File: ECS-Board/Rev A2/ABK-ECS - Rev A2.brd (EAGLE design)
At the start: 80 x 80 mm, 169 parts, among them J1 22-27-2061-06, J2 USB-B-S-RA, J3 1241050-5, J4 MSTBA2, J5 22-05-7068-06, J6 22-05-7028-02, J7 22-05-7068-06, J8 22-05-7028-02, K1 G6K-2G-Y, SW1 B3FS-1015, SW2 B3FS-1015, T1 EXMACHINA-LOGO-NAME, T10 MMBT2222AL, T11 IRLML5103TRPBF, T2 IRLML5103TRPBF, T3 MMBT2222AL, T4 MMBT2222AL, T5 IRLML5103TRPBF, T6 MMBT2222AL, T7 IRLML5103TRPBF, T8 MMBT2222AL, T9 IRLML5103TRPBF, U1 AT24C512C-SSHM-B, U2 LPC1768FBD100, U3 LT3686HDDPBF, U4 LT3686HDDPBF, U5 CD4050BD, X1 FC-135, X2 ASE-12, X3 3000

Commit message: Add rev A2 and modify board
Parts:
- added R75: 1K5, rcl:R0603
- F1: value FUSE3557L -> 1812L110/24DR; device fuse2:3557-LITTLE -> fuse2:LITTLEFUSE_SMD
- moved T1 25.0 mm to (27.3, 62.2)
- moved CC1 10.8 mm to (47.0, 62.2)
- moved R21 2.96 mm to (24.0, 22.1), turned to 270 degrees
- moved R4 1.91 mm to (14.6, 39.4)
- moved R5 1.91 mm to (14.6, 41.7)
- moved R6 1.91 mm to (13.6, 44.5)
- moved LED5 1.62 mm to (25.7, 24.6)
- moved R10 1.27 mm to (17.8, 64.1)
- moved R13 0.90 mm to (29.2, 13.3)
- moved R14 0.90 mm to (10.8, 13.3)
- moved X1 0.90 mm to (21.0, 50.8)
- moved X2 0.90 mm to (21.0, 45.1)
- moved C10 0.90 mm to (17.8, 49.5)
- moved C3 0.90 mm to (17.8, 45.1)
- moved C5 0.90 mm to (17.8, 52.1)
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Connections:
- net MOTOR_CTR renamed R_VALIDATION
- removed net 230V-DETECTION: C20.1, R38.2, U2.43
- removed net VDDA: U2.10
- net +24V: now also F1.2; no longer F1.3, F1.4
- net +3V3: now also R75.1, U2.10
- net 230V_DETECTION: now also C20.1, R38.2
- net N$2: now also R75.2
- net VIN: no longer F1.2
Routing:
- net 230V_DETECTION: track 0.00 -> 51.2 mm, vias 0 -> 2
- net 230V-DETECTION: track 46.2 -> 0.00 mm, vias 2 -> 0
- net GND: track 10.5 -> 23.4 mm, vias 33 -> 31
- net +24V: track 32.0 -> 43.1 mm, vias 13 -> 14
- net +3V3: track 50.3 -> 57.9 mm, vias 33 -> 34
- net N$2: track 3.20 -> 7.47 mm
- net VIN: track 1.40 -> 4.68 mm, vias 1 -> 2
- net USB_D_N: track 18.0 -> 16.1 mm
- net N$1: track 7.55 -> 9.45 mm
- net USB_D_P: track 17.1 -> 15.2 mm
- net XTAL1: track 3.93 -> 5.20 mm
- net N$50: track 1.64 -> 2.71 mm
- net RTCX2: track 7.39 -> 8.29 mm
- net RTCX1: track 8.01 -> 8.91 mm
- net ISP_RXDO: track 37.0 -> 37.7 mm
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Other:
- board text added: "ABK ECS Rev A2"
- board text removed: "ABK ECS Rev A1"

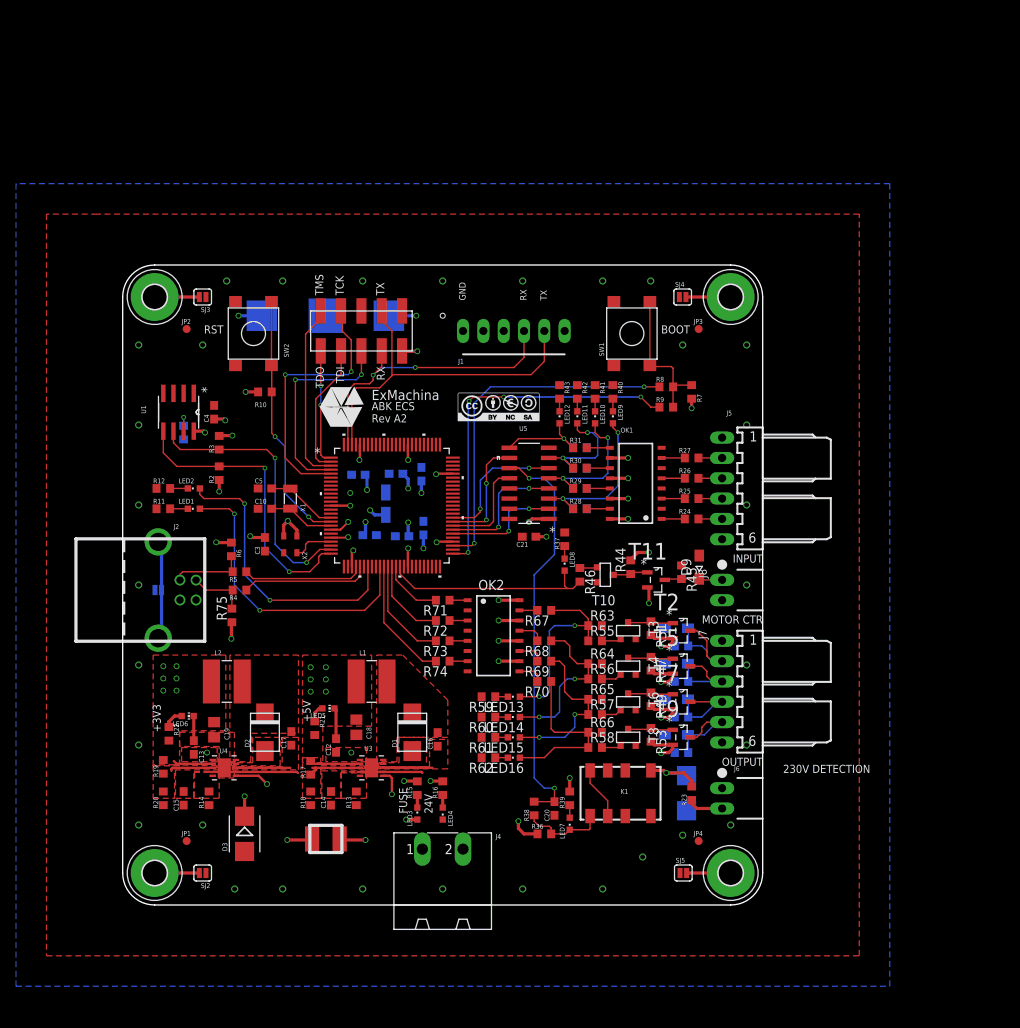
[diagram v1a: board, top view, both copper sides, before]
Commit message: Add input and output to the board and LDO 5V to 3.3V for FTDI connector
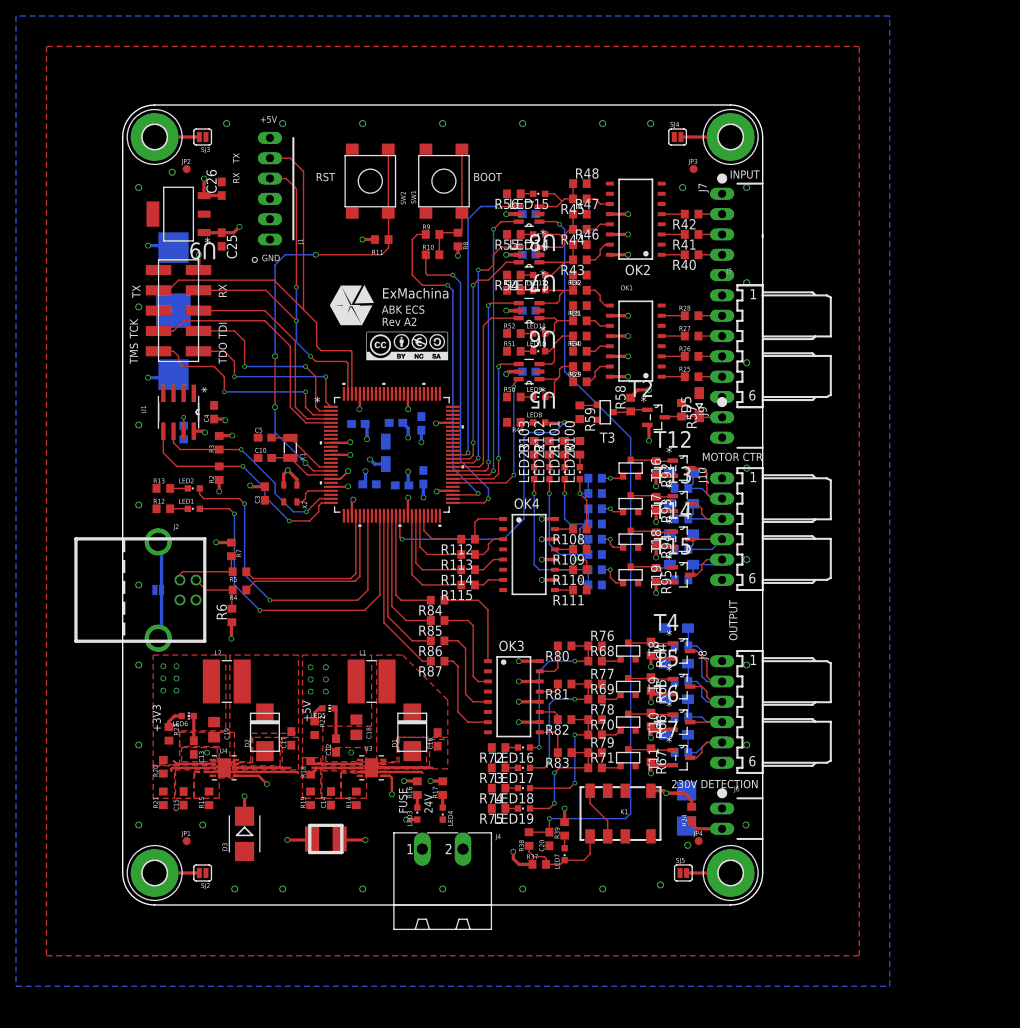
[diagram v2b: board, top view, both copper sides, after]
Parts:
- added C22, C23, C24: 0.1uF, rcl:C0603
- added C25, C26: 1u, rcl:C0603
- added D10, D11, D12, D13: 1N4148WS, diode:SOD323-W
- added J10: 22-05-7068-06, con-molex:7395-06
- added J9: 22-05-7028-02, con-molex:7395-02
- added LED17, LED18, LED19, LED20, LED21, LED22, LED23: Blue, led:CHIPLED_0603
- added OK3, OK4: TLP283-4, optocoupler:MINI-FLAT-16
- added R100, R101, R102, R103: 1K5, rcl:R0603
- added R104, R105, R106, R107, R76, R77, R78, R79: 4K7, rcl:R0603
- added R108, R109, R110, R111, R80, R81, R82, R83: 1K, rcl:R0603
- added R112, R113, R114, R115, R84, R85, R86, R87, R92, R93, R94, R95: 330, rcl:R0603
- added R88, R89, R90, R91: 10K, rcl:R0603
- added R96, R97, R98, R99: 100, rcl:R0603
- added T12, T13, T14, T15: IRLML5103TRPBF, International_Rectifier_By_element14_Batch_1:SOT95P240X112-3N
- added T16, T17, T18, T19: MMBT2222AL, transistor:SOT−23
- added U6, U7, U8: SN74LVC2G17DBVR, ti:SOT95P280X145-6N
- added U9: TC1264-3.3, microchip-6:SOT230P700X180-4N
- J7: value 22-05-7068-06 -> 22-05-7058-05; device con-molex:7395-06 -> con-molex:7395-05
- J8: value 22-05-7028-02 -> 22-05-7068-06; device con-molex:7395-02 -> con-molex:7395-06
- R10: value 10K -> 0R
- R11, R21, R60, R61, R62: value 1K5 -> 10K
- R13: value 31K6 -> 1K5
- R15: value 4K7 -> 31K6
- R17: value 52K3 -> 4K7
- R18: value 10K -> 52K3
- R19: value 31K6 -> 10K
- R20: value 10K -> 31K6
- R23, R55, R56: value 100 -> 1K5
- R24, R68, R69, R70: value 1K -> 100
- R32: value 4K7 -> 1K
- R37: value 1K5 -> 4K7
- R40, R41, R42, R43: value 1K5 -> 1K
- R44: value 330 -> 1K
- R45: value 10K -> 1K
- R46: value 100 -> 4K7
- R47: value 330 -> 4K7
- R48: value 10K -> 4K7
- R49, R51, R53, R72, R73, R74: value 330 -> 1K5
- R50, R52, R54, R7: value 10K -> 1K5
- R57: value 100 -> 10K
- R58: value 100 -> 330
- R59: value 1K5 -> 100
- R63: value 4K7 -> 10K
- R64, R65, R66: value 4K7 -> 330
- R67: value 1K -> 330
- R71: value 330 -> 100
- R8: value 0R -> 10K
- T11, T9: value IRLML5103TRPBF -> MMBT2222AL; device International_Rectifier_By_element14_Batch_1:SOT95P240X112-3N -> transistor:SOT−23
- T4, T6: value MMBT2222AL -> IRLML5103TRPBF; device transistor:SOT−23 -> International_Rectifier_By_element14_Batch_1:SOT95P240X112-3N
- U5: value CD4050BD -> SN74LVC2G17DBVR; device TI-CD4050BD:SOIC127P600X175-16N -> ti:SOT95P280X145-6N
- moved R36 70.0 mm to (57.1, 78.7)
- moved LED15 68.0 mm to (52.1, 88.9)
- moved R23 65.8 mm to (5.78, 21.4), turned to 270 degrees
- moved R48 63.5 mm to (57.1, 90.2), flipped to the top, turned to 0 degrees
- moved R54 63.3 mm to (48.9, 78.7), flipped to the top
- moved R56 61.5 mm to (48.9, 88.9), turned to 180 degrees
- moved R7 60.8 mm to (13.6, 44.5)
- moved LED14 60.4 mm to (52.1, 83.8)
- moved R53 58.1 mm to (48.9, 76.8), turned to 180 degrees
- moved J7 57.1 mm to (74.9, 83.8)
- moved R47 56.9 mm to (57.1, 86.4), turned to 0 degrees
- moved OK2 55.0 mm to (64.1, 85.7), turned to 180 degrees
- moved LED13 52.8 mm to (52.1, 78.7)
- moved R52 52.3 mm to (48.9, 71.4), flipped to the top
- moved R55 51.8 mm to (48.9, 83.8), turned to 180 degrees
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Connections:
- new net INPUT: LED15.A, R45.2, R48.1, U8.3
- new net INPUT_MCU: U2.63, U8.4
- new net LED1: D10.C, J10.2, R88.2, T12.3
- new net LED1_MCU: R112.2, U2.46
- new net LED2: D11.C, J10.3, R89.2, T13.3
- new net LED2_MCU: R113.2, U2.45
- new net LED3: D12.C, J10.4, R90.2, T14.3
- new net LED3_MCU: R114.2, U2.44
- new net LED4: D13.C, J10.5, R91.2, T15.3
- new net LED4_MCU: R115.2, U2.43
- new net N$100: OK2.15, R43.1
- new net N$101: OK2.3, R41.2
- new net N$102: J7.3, R41.1
- new net N$103: OK2.13, R44.1
- new net N$104: OK2.5, R42.2
- new net N$105: J7.2, R42.1
- new net N$106: OK2.11, R45.1
- new net N$107: LED13.C, R54.1
- new net N$108: LED14.C, R55.1
- new net N$109: LED15.C, R56.1
- new net N$31: LED20.A, R104.1, R108.1, R96.1
- new net N$33: OK4.15, R108.2
- new net N$34: LED21.A, R105.1, R109.1, R97.1
- new net N$35: OK4.13, R109.2
- new net N$36: LED22.A, R106.1, R110.1, R98.1
- new net N$37: LED23.A, R107.1, R111.1, R99.1
- new net N$38: OK4.11, R110.2
- new net N$39: OK4.9, R111.2
- new net N$40: OK4.1, R112.1
- new net N$42: OK4.3, R113.1
- new net N$43: OK4.7, R115.1
- new net N$46: OK4.5, R114.1
- new net N$66: LED20.C, R100.1
- new net N$67: LED21.C, R101.1
- new net N$68: LED22.C, R102.1
- new net N$69: LED23.C, R103.1
- new net N$71: R92.1, T12.1, T16.3
- new net N$72: R93.1, T13.1, T17.3
- new net N$77: R94.1, T14.1, T18.3
- new net N$78: R95.1, T15.1, T19.3
- new net N$81: OK2.1, R40.2
- new net N$82: J7.4, R40.1
- new net N$84: R96.2, T16.1
- new net N$85: R97.2, T17.1
- new net N$98: R98.2, T18.1
- new net N$99: R99.2, T19.1
- new net SLOWFEED_1: LED13.A, R43.2, R46.1, U7.1
- new net SLOWFEED_1_MCU: U2.62, U7.6
- new net SLOWFEED_2: LED14.A, R44.2, R47.1, U7.3
- new net SLOWFEED_2_MCU: U2.61, U7.4
- net !RESET: now also R11.1; no longer R10.1
- net +24V: now also J10.1, J8.1, R17.2, R58.2, R64.2, R65.2, R66.2, R67.2, R92.2, R93.2, R94.2, R95.2, T12.2, T13.2, T14.2, T15.2, T4.2, T6.2; no longer R15.2, R44.2, R47.2, R49.2, R51.2, R53.2, T11.2, T9.2
- net +3V3: now also C22.1, C23.1, C24.1, C26.1, R11.2, R20.2, R23.2, R7.1, R8.2, U5.5, U6.5, U7.5, U8.5, U9.3; no longer R10.2, R19.2, R22.2, R7.2, R75.1, U5.1
- net +5V: now also C25.1, J1.6, OK3.10, OK3.12, OK3.14, OK3.16, OK4.10, OK4.12, OK4.14, OK4.16, R18.2, R22.2, R37.1, U9.1; no longer OK2.10, R17.2, R21.2, R36.1
- net 230V_DETECTION: now also U8.1; no longer U5.11
- net 230V_DETECTION_MCU: now also U8.6; no longer U5.12
- net BOOT_SELECT_P2_10: now also R9.1; no longer R8.1
- net BOOT_SELECT_P2_12: now also R10.1; no longer R9.1
- net BRAKE_CONTROL: now also D9.C, J8.5, R63.2, T7.3; no longer D8.C, J7.5, R54.2, T9.3
- net BRAKE_CONTROL_MCU: now also R87.2; no longer R74.2
- net CLUTCH_CONTROL: now also D8.C, J8.4, R62.2, T6.3; no longer D7.C, J7.4, R52.2, T7.3
- net CLUTCH_CONTROL_MCU: now also R86.2; no longer R73.2
- net DRIVE_STATUS_1: now also R31.2, R35.1, U6.1; no longer R30.2, R34.1, U5.7
- net DRIVE_STATUS_1_MCU: now also U6.6; no longer U5.6
- net DRIVE_STATUS_2: now also R32.2, R36.1, U6.3; no longer R31.2, R35.1, U5.9
- net DRIVE_STATUS_2_MCU: now also U6.4; no longer U5.10
- net EMERGENCY_STOP: now also R29.2, R33.1, U5.1; no longer R28.2, R32.1, U5.3
- net EMERGENCY_STOP_MCU: now also U5.6; no longer U5.2
- net GND: now also C22.2, C23.2, C24.2, C25.2, C26.2, D10.A, D11.A, D12.A, D13.A, J10.6, J7.5, J8.6, J9.2, OK3.2, OK3.4, OK3.6, OK3.8, OK4.2, OK4.4, OK4.6, OK4.8, R100.2, R101.2, R102.2, R103.2, R104.2, R105.2, R106.2, R107.2, R13.2, R15.1, R19.1, R21.1, R36.2, R46.2, R47.2, R48.2, R49.2, R50.2, R51.2, R52.2, R53.2, R54.2, R55.2, R56.2, R57.1, R60.1, R61.1, R62.1, R63.1, R72.2, R73.2, R74.2, R75.2, R76.2, R77.2, R78.2, R79.2, R88.1, R89.1, R90.1, R91.1, T11.2, T16.2, T17.2, T18.2, T19.2, T9.2, U5.2, U6.2, U7.2, U8.2, U9.2, U9.4; no longer J7.6, J8.2, OK2.8, R11.2, R13.1, R18.1, R20.1, R32.2, R37.2, R40.2, R41.2, R42.2, R43.2, R45.1, R48.1, R50.1, R52.1, R54.1, R59.2, R60.2, R61.2, R62.2, R63.2, R64.2, R65.2, R66.2, T4.2, T6.2, U5.8
- net LIMIT_SWITCH: now also R30.2, R34.1, U5.3; no longer R29.2, R33.1, U5.5
- net L_VALIDATION: now also D7.C, J8.3, R61.2; no longer D6.C, J7.3, R48.2
- net L_VALIDATION_MCU: now also R85.2; no longer R72.2
- net MOTOR_CONTROL_MCU: now also R59.2; no longer R46.2
- net N$1: now also R7.2; no longer R6.2
- net N$13: now also R20.1, R21.2; no longer R19.1, R20.2
- net N$17: now also R68.2, T8.1; no longer R55.2, T3.1
- net N$18: now also R64.1, T4.1, T8.3; no longer R51.1, T2.1, T3.3
- net N$19: now also R69.2, T9.1; no longer R56.2, T4.1
- net N$2: now also R6.2; no longer R75.2
- net N$20: now also R65.1, T9.3; no longer R47.1, T4.3
- net N$21: now also R70.2, T10.1; no longer R57.2, T6.1
- net N$22: now also R66.1, T10.3, T6.1; no longer R49.1, T6.3, T7.1
- net N$23: now also R71.2, T11.1; no longer R58.2, T8.1
- net N$24: now also R67.1, T11.3, T7.1; no longer R53.1, T8.3, T9.1
- net N$25: now also R59.1, T3.1; no longer R46.1, T10.1
- net N$26: now also R58.1, T2.1, T3.3; no longer R44.1, T10.3, T11.1
- net N$28: now also R24.2; no longer R23.2
- net N$29: now also R12.1; no longer R11.1
- net N$3: now also R13.1; no longer R12.1
- net N$30: now also D5.C, J9.1, R57.2, T2.3; no longer D9.C, J8.1, R45.2, T11.3
- net N$32: now also R24.1; no longer R23.1
- net N$4: now also R14.2; no longer R13.2
- net N$41: now also R25.2; no longer R24.2
- net N$44: now also R17.1; no longer R16.1
- net N$45: now also R16.1; no longer R15.1
- net N$47: now also R26.2; no longer R25.2
- net N$48: now also R27.2; no longer R26.2
- net N$49: now also R28.2; no longer R27.2
- net N$5: now also R10.2, R8.1; no longer R7.1, R8.2
- net N$50: now also R23.1; no longer R22.1
- net N$51: now also R22.1; no longer R21.1
- net N$52: now also R28.1; no longer R27.1
- net N$53: now also R27.1; no longer R26.1
- net N$54: now also R26.1; no longer R25.1
- net N$55: now also R25.1; no longer R24.1
- net N$56: now also R49.1; no longer R37.1
- net N$57: now also R50.1; no longer R40.1
- net N$58: now also R51.1; no longer R41.1
- net N$59: now also R52.1; no longer R42.1
- net N$61: now also R32.1; no longer R31.1
- net N$62: now also R31.1; no longer R30.1
- net N$63: now also R30.1; no longer R29.1
- net N$64: now also R29.1; no longer R28.1
- net N$65: now also R53.1; no longer R43.1
- net N$7: now also R15.2; no longer R14.2
- net N$73: now also R37.2; no longer R36.2
- net N$75: now also LED16.A, R68.1, R76.1, R80.1; no longer LED13.A, R55.1, R63.1, R67.1
- net N$76: now also OK3.15, R80.2; no longer OK2.15, R67.2
- net N$79: now also LED17.A, R69.1, R77.1, R81.1; no longer LED14.A, R56.1, R64.1, R68.1
- net N$80: now also OK3.13, R81.2; no longer OK2.13, R68.2
- net N$83: now also LED18.A, R70.1, R78.1, R82.1; no longer LED15.A, R57.1, R65.1, R69.1
- net N$86: now also LED19.A, R71.1, R79.1, R83.1; no longer LED16.A, R58.1, R66.1, R70.1
- net N$87: now also OK3.11, R82.2; no longer OK2.11, R69.2
- net N$88: now also OK3.9, R83.2; no longer OK2.9, R70.2
- net N$89: now also OK3.1, R84.1; no longer OK2.1, R71.1
- net N$9: now also R18.1, R19.2; no longer R17.1, R18.2
- net N$91: now also OK3.3, R85.1; no longer OK2.3, R72.1
- net N$92: now also OK3.7, R87.1; no longer OK2.7, R74.1
- net N$93: now also OK3.5, R86.1; no longer OK2.5, R73.1
- net N$94: now also LED16.C, R72.1; no longer LED13.C, R59.1
- net N$95: now also LED17.C, R73.1; no longer LED14.C, R60.1
- net N$96: now also LED18.C, R74.1; no longer LED15.C, R61.1
- net N$97: now also LED19.C, R75.1; no longer LED16.C, R62.1
- net R_VALIDATION: now also D6.C, J8.2, R60.2, T4.3; no longer D5.C, J7.2, R50.2, T2.3
- net R_VALIDATION_MCU: now also R84.2; no longer R71.2
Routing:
- net +5V: track 31.1 -> 110.8 mm, vias 16 -> 24
- net 230V_DETECTION: track 51.2 -> 94.6 mm
- net INPUT_MCU: track 0.00 -> 38.2 mm, vias 0 -> 2
- net SLOWFEED_2_MCU: track 0.00 -> 33.9 mm, vias 0 -> 2
- net SLOWFEED_1_MCU: track 0.00 -> 30.9 mm, vias 0 -> 2
- net 230V_DETECTION_MCU: track 12.3 -> 39.0 mm, vias 0 -> 2
- net !RESET: track 31.9 -> 57.3 mm, vias 2 -> 4
- net N$37: track 0.00 -> 22.6 mm, vias 0 -> 2
- net N$36: track 0.00 -> 19.0 mm, vias 0 -> 2
- net +3V3: track 57.9 -> 75.4 mm, vias 34 -> 37
- net DRIVE_STATUS_2_MCU: track 14.4 -> 28.8 mm
- net N$34: track 0.00 -> 14.3 mm, vias 0 -> 2
- net LED4_MCU: track 0.00 -> 14.1 mm
- net LED1: track 0.00 -> 14.0 mm
- net MOTOR_CONTROL_MCU: track 26.9 -> 39.9 mm, vias 0 -> 2
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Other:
- board size 80 x 80 mm -> 80 x 100 mm

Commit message: Rotate board 90 degres
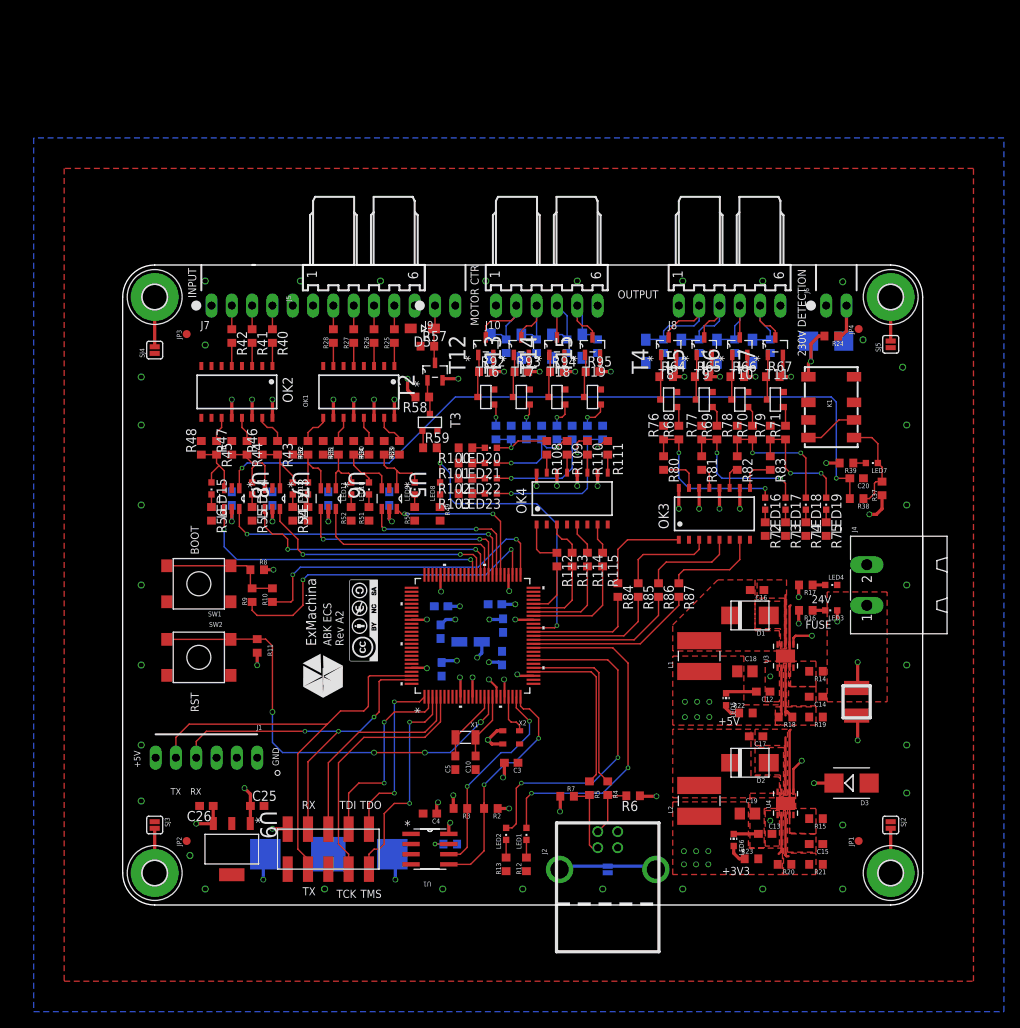
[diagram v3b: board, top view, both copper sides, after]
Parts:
- moved MP1 92.0 mm to (96.0, 4.00), turned to 90 degrees
- moved MP2 92.0 mm to (4.00, 4.00), turned to 90 degrees
- moved SJ2 86.2 mm to (96.0, 10.0), turned to 270 degrees
- moved SJ3 86.2 mm to (4.00, 10.0), turned to 270 degrees
- moved JP1 84.0 mm to (92.0, 8.00), turned to 90 degrees
- moved JP2 84.0 mm to (8.00, 8.00), turned to 90 degrees
- moved R21 82.0 mm to (86.7, 5.08), turned to 180 degrees
- moved U9 79.7 mm to (13.6, 6.99), turned to 270 degrees
- moved C15 79.3 mm to (86.7, 7.62), turned to 0 degrees
- moved R20 78.6 mm to (82.7, 5.08), turned to 180 degrees
- moved C26 77.2 mm to (10.5, 12.4), turned to 180 degrees
- moved D3 76.1 mm to (91.1, 15.2), turned to 0 degrees
- moved R15 75.9 mm to (86.7, 10.8), turned to 180 degrees
- moved MP3 74.7 mm to (4.00, 76.0), turned to 90 degrees
- moved MP4 74.7 mm to (96.0, 76.0), turned to 90 degrees
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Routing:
- added copper zone on layer 1, net VIN
- removed copper zone on layer 15, net VIN
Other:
- board size 80 x 100 mm -> 100 x 80 mm

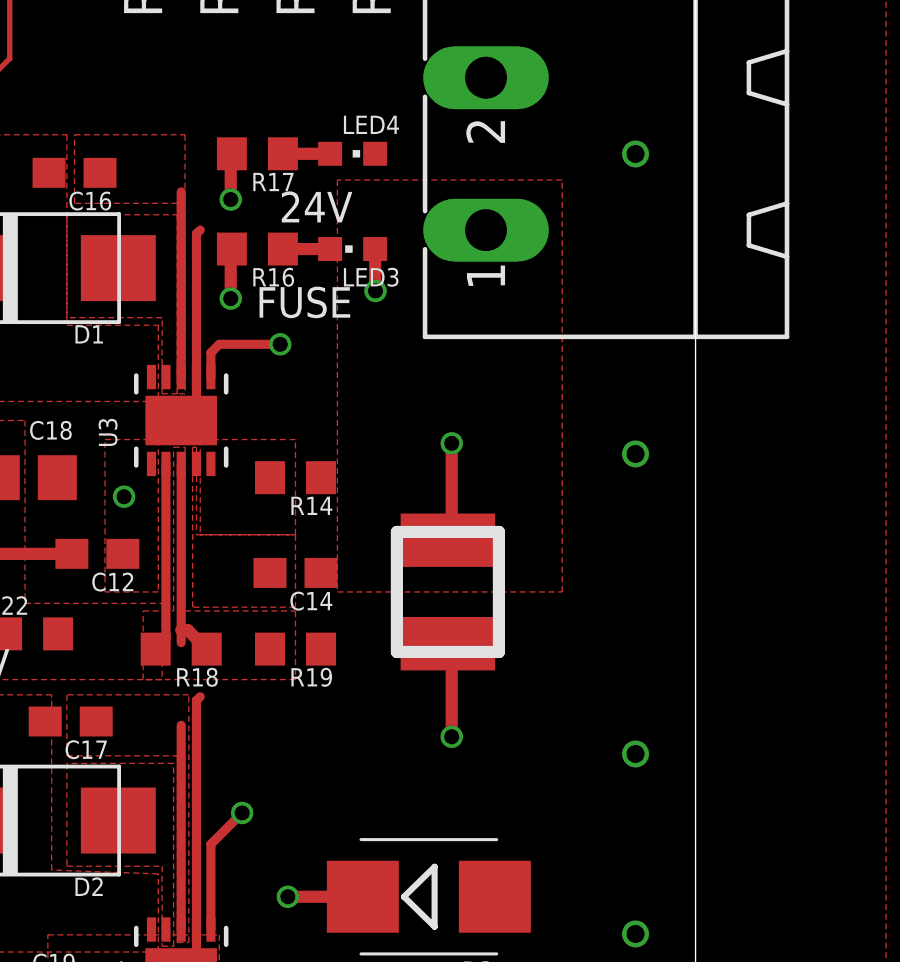
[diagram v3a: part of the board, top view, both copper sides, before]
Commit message: Add 24V and Vin poly for the fuse
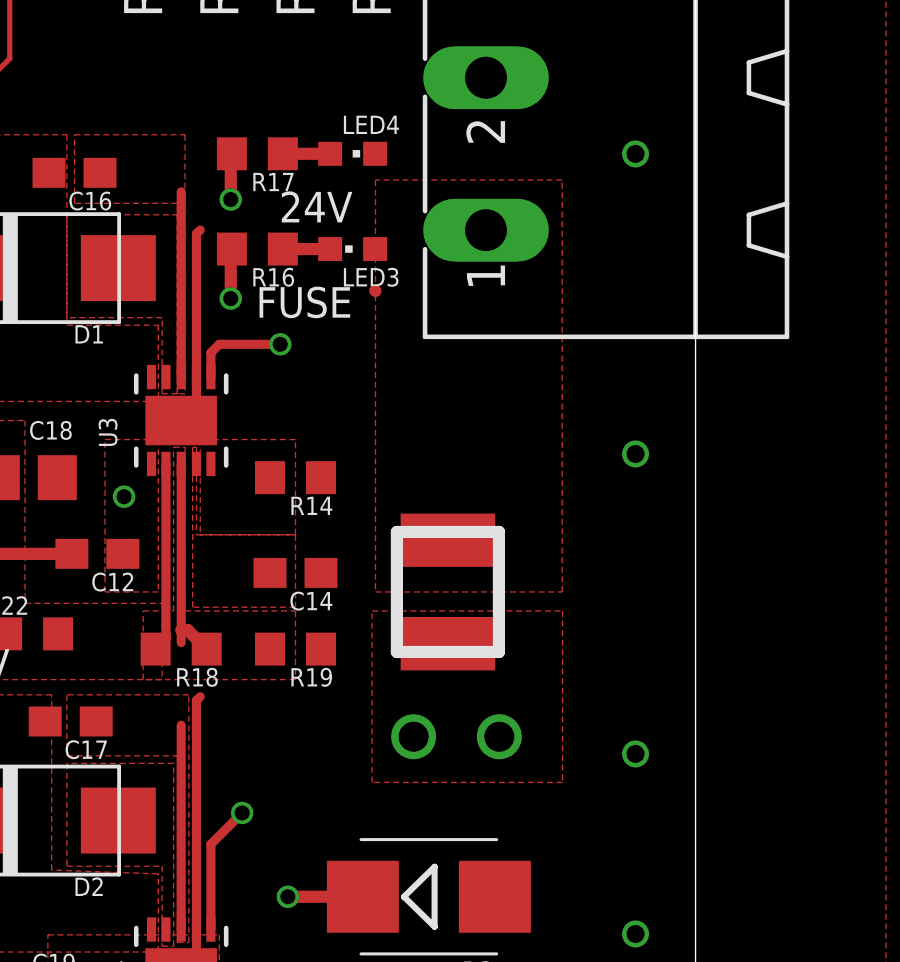
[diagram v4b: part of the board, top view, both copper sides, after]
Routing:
- net VIN: track 4.68 -> 0.20 mm, vias 2 -> 0
- net +24V: track 54.4 -> 51.5 mm, vias 18 -> 19
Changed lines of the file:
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@@
 <setting verticaltext="up"/>
 </settings>
-<grid distance="1" unitdist="mm" unit="mm" style="lines" multiple="2" display="yes" altdistance="12.5" altunitdist="mil" altunit="mil"/>
+<grid distance="25" unitdist="mil" unit="mil" style="lines" multiple="2" display="yes" altdistance="12.5" altunitdist="mil" altunit="mil"/>
 <layers>
 <layer number="1" name="Top" color="16" fill="1" visible="yes" active="yes"/>
@@
 <contactref element="F1" pad="1"/>
 <contactref element="LED3" pad="A"/>
-<polygon width="0.4064" layer="1">
-<vertex x="88.062" y="25.4"/>
+<polygon width="0.762" layer="1">
+<vertex x="89.332" y="25.4"/>
 <vertex x="95.555" y="25.4"/>
 <vertex x="95.555" y="39.132"/>
-<vertex x="88.062" y="39.132"/>
+<vertex x="89.332" y="39.132"/>
 </polygon>
-<via x="89.332" y="35.433" extent="1-16" drill="0.5"/>
 <wire x1="89.332" y1="35.433" x2="89.32" y2="35.445" width="0.4064" layer="1"/>
-<wire x1="89.32" y1="35.445" x2="89.32" y2="36.83" width="0.4064" layer="1"/>
-<via x="91.872" y="30.353" extent="1-16" drill="0.5"/>
 <wire x1="91.745" y1="27.125" x2="91.872" y2="27.252" width="0.4064" layer="1"/>
-<wire x1="91.872" y1="27.252" x2="91.872" y2="30.353" width="0.4064" layer="1"/>
 </signal>
 <signal name="N$44">
@@
 <vertex x="82.093" y="7.366"/>
 </polygon>
-<polygon width="0.4064" layer="15" rank="3">
+<polygon width="0.762" layer="15" rank="3">
 <vertex x="96.825" y="67.945"/>
 <vertex x="96.825" y="9.398"/>
@@
 <wire x1="83.8456" y1="33.3756" x2="84.125" y2="33.655" width="0.3048" layer="1"/>
 <wire x1="84.125" y1="33.655" x2="86.157" y2="33.655" width="0.3048" layer="1"/>
-<via x="91.872" y="20.574" extent="1-16" drill="0.5"/>
 <wire x1="91.745" y1="23.675" x2="91.872" y2="23.548" width="0.4064" layer="1"/>
-<wire x1="91.872" y1="23.548" x2="91.872" y2="20.574" width="0.4064" layer="1"/>
 <contactref element="J10" pad="1"/>
 <contactref element="R92" pad="2"/>
@@
 <wire x1="59.6648" y1="68.7578" x2="59.6648" y2="66.7648" width="0.4064" layer="1"/>
 <wire x1="59.6648" y1="66.7648" x2="59.575" y2="66.675" width="0.4064" layer="1"/>
+<via x="90.602" y="20.574" extent="1-16" drill="1"/>
+<via x="93.4595" y="20.574" extent="1-16" drill="1"/>
+<polygon width="0.762" layer="1" rank="2">
+<vertex x="89.2175" y="19.05"/>
+<vertex x="89.2175" y="24.765"/>
+<vertex x="95.5675" y="24.765"/>
+<vertex x="95.5675" y="19.05"/>
+</polygon>
 </signal>
 <signal name="+5V" class="2">
